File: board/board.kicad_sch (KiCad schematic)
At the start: 1 part

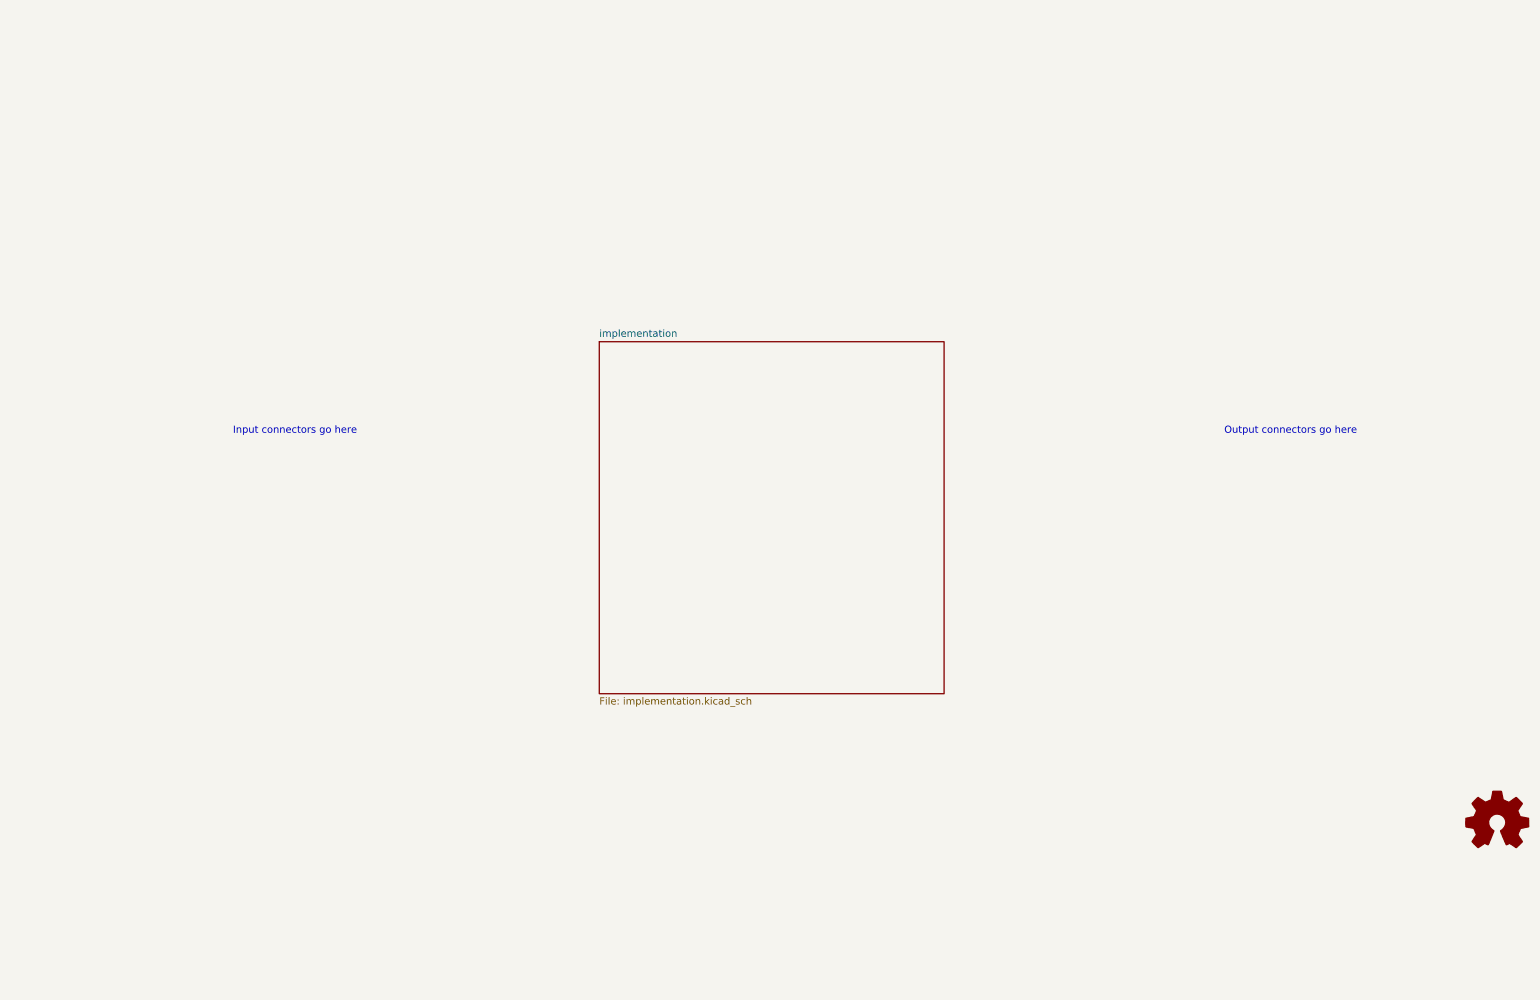
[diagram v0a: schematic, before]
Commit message: modernized the legacy version
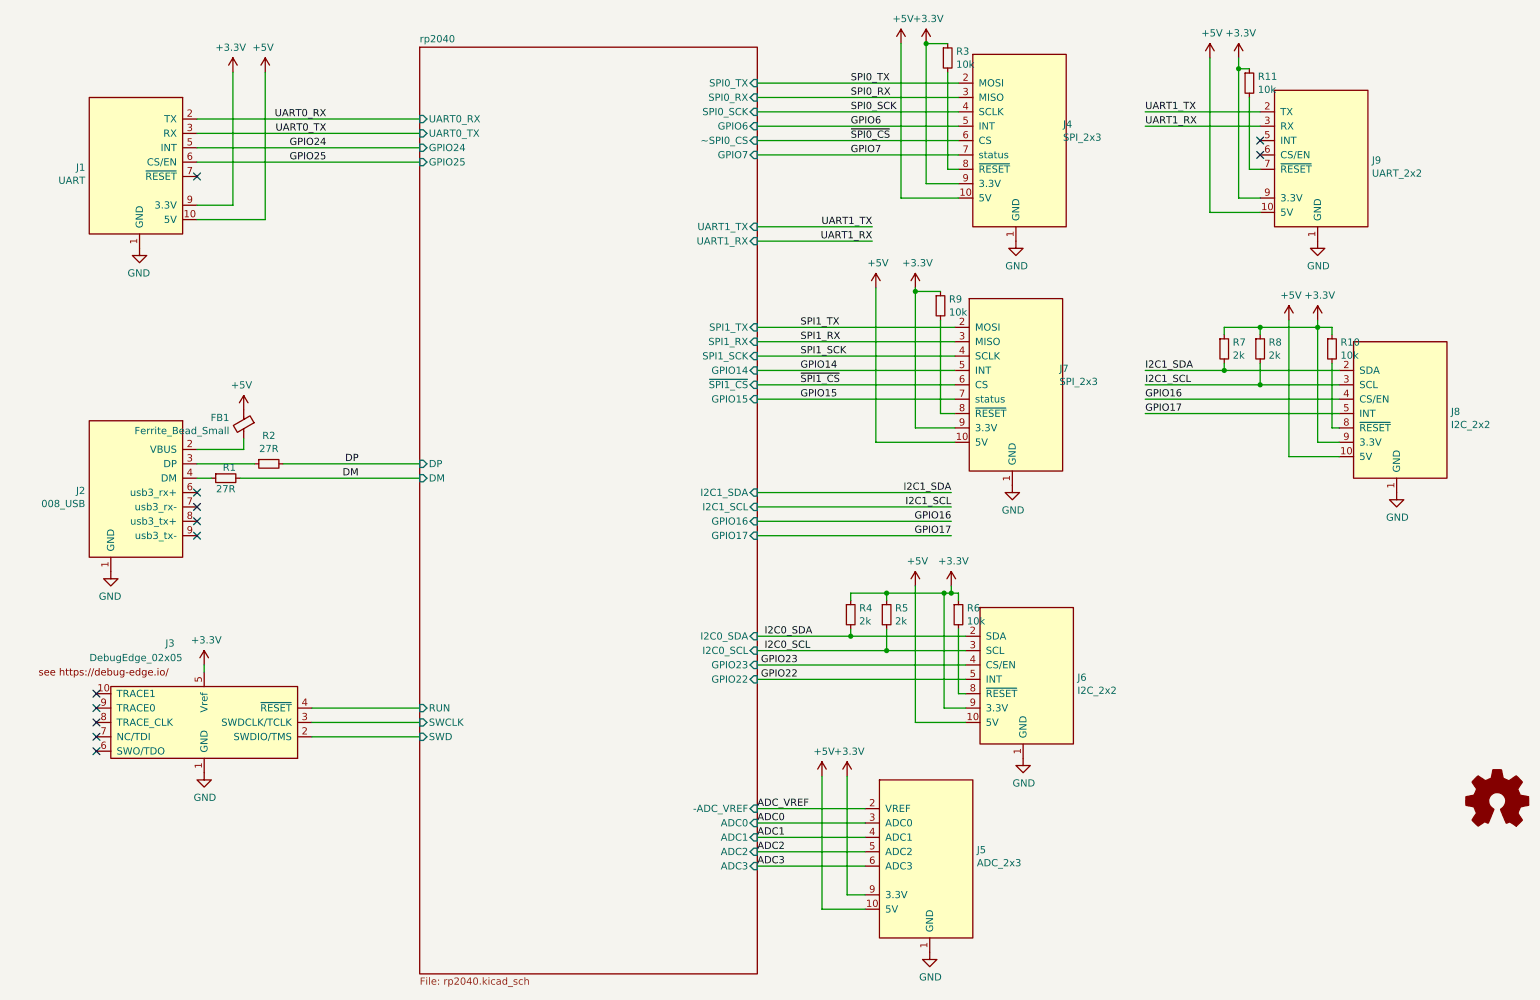
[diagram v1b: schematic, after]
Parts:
- added FB1: Ferrite_Bead_Small, Inductor_SMD:L_0805_2012Metric, symbol Device:FerriteBead_Small
- added J1: UART, on_edge:on_edge_2x05_device, symbol put_on_edge:010_UART
- added J2: 008_USB, on_edge:on_edge_2x05_device, symbol put_on_edge:008_USB
- added J3: DebugEdge_02x05, on_edge:debug_edge_2x05_device, symbol put_on_edge:DebugEdge_02x05
- added J4: SPI_2x3, on_edge:on_edge_2x05_up_host, symbol put_on_edge:002_SPI
- added J5: ADC_2x3, on_edge:on_edge_2x05_host, symbol put_on_edge:007_ADC
- added J6: I2C_2x2, on_edge:on_edge_2x05_up_host, symbol put_on_edge:001_I2C
- added J7: SPI_2x3, on_edge:on_edge_2x05_host, symbol put_on_edge:002_SPI
- added J8: I2C_2x2, on_edge:on_edge_2x05_host, symbol put_on_edge:001_I2C
- added J9: UART_2x2, on_edge:on_edge_2x05_host, symbol put_on_edge:010_UART
- added R1, R2: 27R, Resistor_SMD:R_0603_1608Metric, symbol Device:R_Small
- added R10, R11, R3, R6, R9: 10k, Resistor_SMD:R_0603_1608Metric, symbol Device:R_Small
- added R4, R5, R7, R8: 2k, Resistor_SMD:R_0603_1608Metric, symbol Device:R_Small
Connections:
- new net: J9.7 (~{RESET}), R11.2
- new net: J7.8 (~{RESET}), R9.2
- new net: J2.4 (DM), R1.1
- new net: J4.8 (~{RESET}), R3.2
- new net: J8.8 (~{RESET}), R10.2
- new net: J6.8 (~{RESET}), R6.2
- new net: J2.3 (DP), R2.1
- new net: FB1.2, J2.2 (VBUS)
- new net +3V3: J1.9 (3.3V), J3.5 (Vref), J4.9 (3.3V), J5.9 (3.3V), J6.9 (3.3V), J7.9 (3.3V), J8.9 (3.3V), J9.9 (3.3V), R10.1, R11.1, R3.1, R4.1, R5.1, R6.1, R7.1, R8.1, R9.1
- new net +5V: FB1.1, J1.10 (5V), J4.10 (5V), J5.10 (5V), J6.10 (5V), J7.10 (5V), J8.10 (5V), J9.10 (5V)
- new net ADC0: J5.3 (ADC0)
- new net ADC1: J5.4 (ADC1)
- new net ADC2: J5.5 (ADC2)
- new net ADC3: J5.6 (ADC3)
- new net ADC_VREF: J5.2 (VREF)
- new net DM: R1.2
- new net DP: R2.2
- new net GND: J1.1 (GND), J2.1 (GND), J3.1 (GND), J4.1 (GND), J5.1 (GND), J6.1 (GND), J7.1 (GND), J8.1 (GND), J9.1 (GND)
- new net GPIO14: J7.5 (INT)
- new net GPIO15: J7.7 (status)
- new net GPIO16: J8.4 (CS/EN)
- new net GPIO17: J8.5 (INT)
- new net GPIO22: J6.5 (INT)
- new net GPIO23: J6.4 (CS/EN)
- new net GPIO24: J1.5 (INT)
- new net GPIO25: J1.6 (CS/EN)
- new net GPIO6: J4.5 (INT)
- new net GPIO7: J4.7 (status)
- new net I2C0_SCL: J6.3 (SCL), R5.2
- new net I2C0_SDA: J6.2 (SDA), R4.2
- new net I2C1_SCL: J8.3 (SCL), R8.2
- new net I2C1_SDA: J8.2 (SDA), R7.2
- new net SPI0_RX: J4.3 (MISO)
- new net SPI0_SCK: J4.4 (SCLK)
- new net SPI0_TX: J4.2 (MOSI)
- new net SPI1_RX: J7.3 (MISO)
- new net SPI1_SCK: J7.4 (SCLK)
- new net SPI1_TX: J7.2 (MOSI)
- new net UART0_RX: J1.2 (TX)
- new net UART0_TX: J1.3 (RX)
- new net UART1_RX: J9.3 (RX)
- new net UART1_TX: J9.2 (TX)
- new net rp2040/RUN: J3.4 (~{RESET})
- new net rp2040/SWCLK: J3.3 (SWDCLK/TCLK)
- new net rp2040/SWD: J3.2 (SWDIO/TMS)
- new net ~{SPI0_CS}: J4.6 (CS)
- new net ~{SPI1_CS}: J7.6 (CS)
- no-connect marks 0 -> 12
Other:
- sheet implementation renamed rp2040
- sheet rp2040: file implementation.kicad_sch -> rp2040.kicad_sch
- sheet rp2040 ports: added ADC0, ADC1, ADC2, ADC3, DM, DP, GPIO14, GPIO15, GPIO16, GPIO17, GPIO22, GPIO23, GPIO24, GPIO25, GPIO6, GPIO7, I2C0_SCL, I2C0_SDA, I2C1_SCL, I2C1_SDA, RUN, SPI0_RX, SPI0_SCK, SPI0_TX, SPI1_RX, SPI1_SCK, SPI1_TX, SWCLK, SWD, UART0_RX, UART0_TX, UART1_RX, UART1_TX, ~SPI0_CS, ~{SPI1_CS}, ­ADC_VREF; removed none
- note removed: "Input connectors go here"
- note removed: "Output connectors go here"
